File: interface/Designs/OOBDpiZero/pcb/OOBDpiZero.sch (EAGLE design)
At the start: 120 parts, among them IC10 STM32F042CT, IC11 EEPROM24, IC20 GL850G-31, IC3 DS3231, IC4 MC34063-SO, Q2 12MHz, U1 SN65HVD230(SO8), U11 STM32F042CT, U2 SN65HVD230(SO8), U4 SY6280

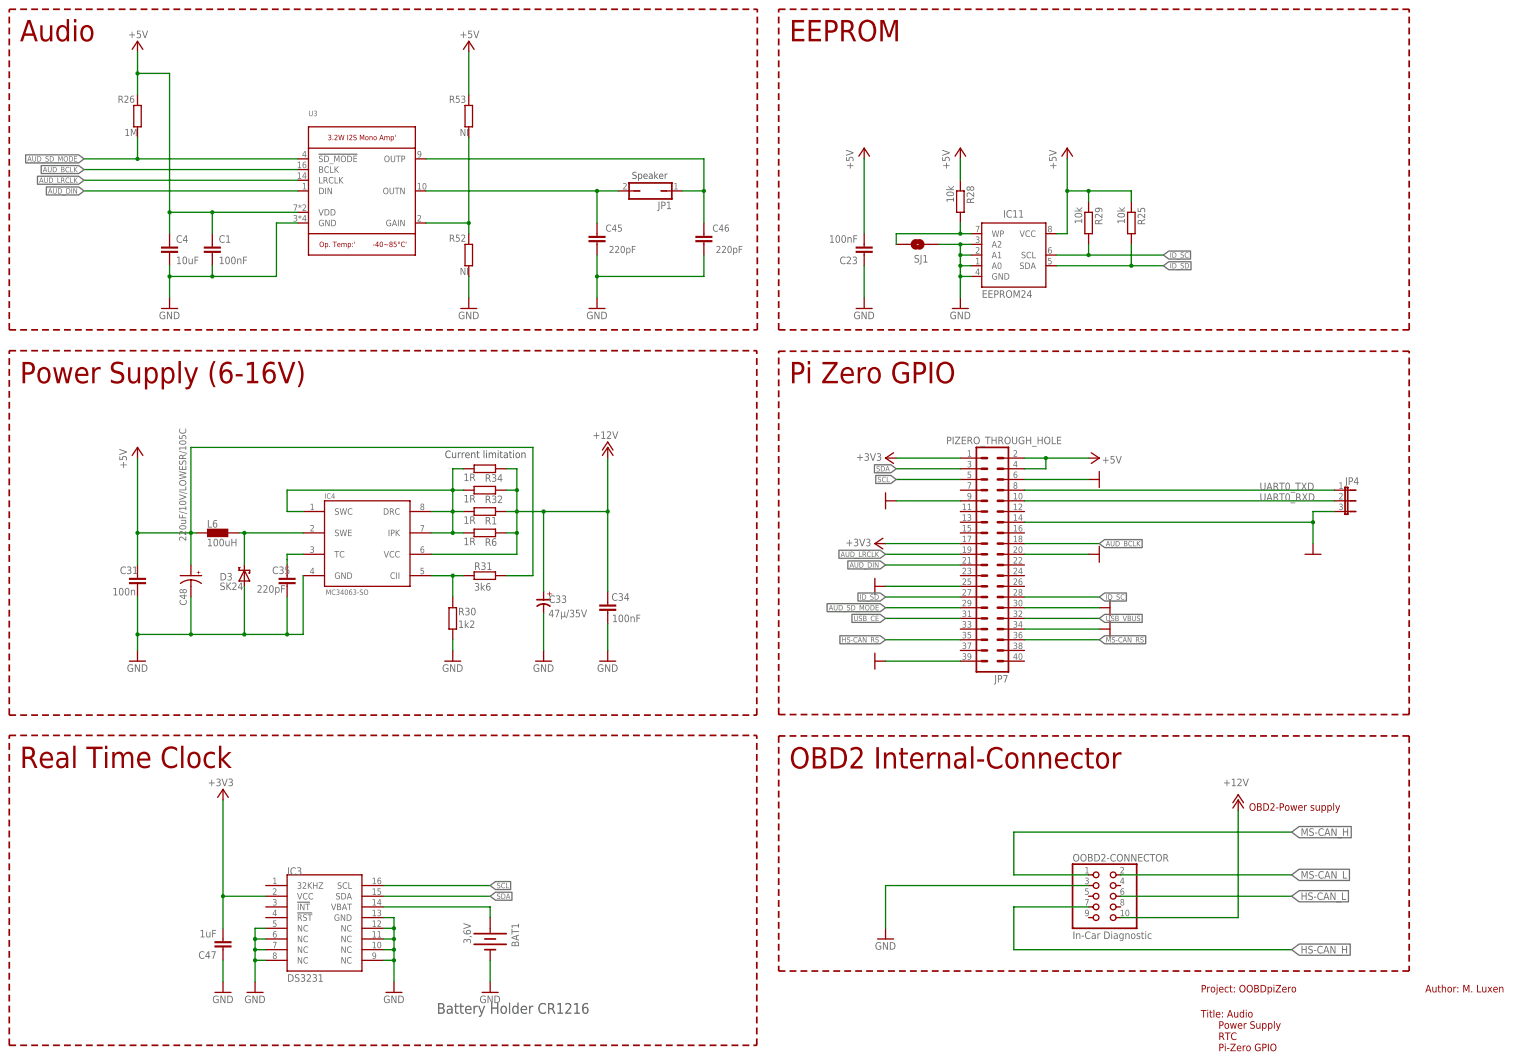
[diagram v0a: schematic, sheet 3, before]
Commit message: correct last faulty stashed commit
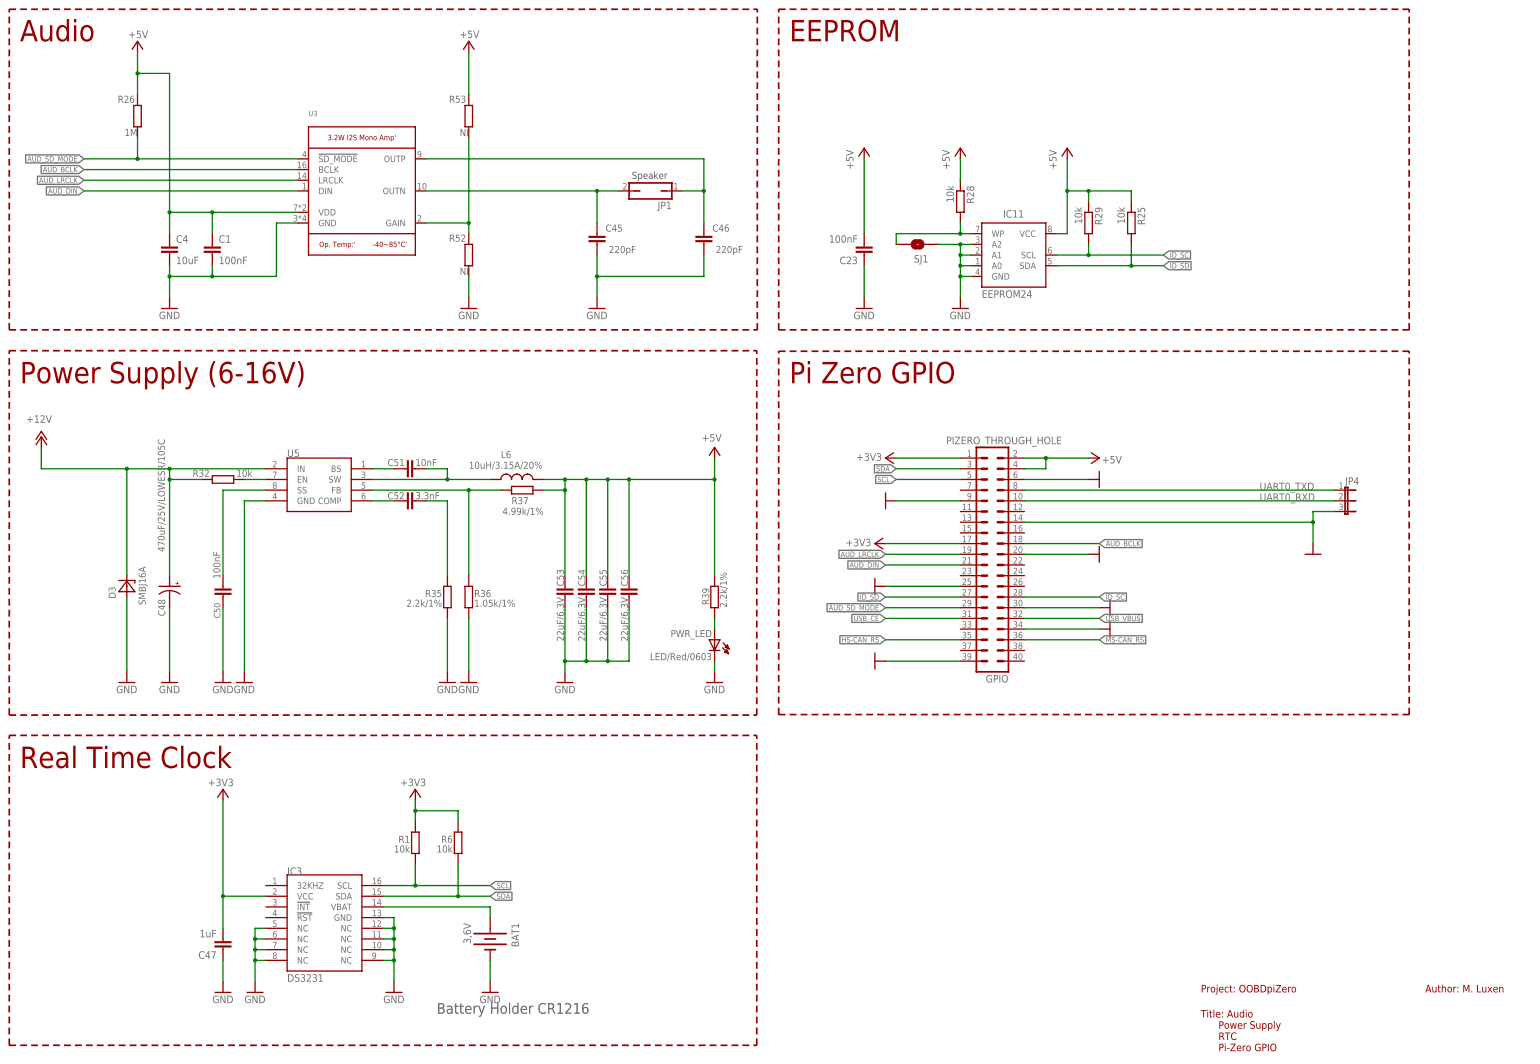
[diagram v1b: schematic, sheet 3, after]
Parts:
- removed C31: 100n, rcl:C-EUC0603K
- removed C33: 47µ/35V, cap-master:CP-SV-D
- removed C34: 100nF, rcl:C-EUC0603K
- removed C35: 220pF, rcl:C-EUC0603K
- removed IC4: MC34063-SO, mc34063:MC34063-SO
- removed OOBD2-CONNECTOR: In-Car Diagnostic, pinhead:PINHD-2X5/90
- removed R30: 1k2, rcl:R-EU_R0603
- removed R31: 3k6, rcl:R-EU_R0603
- removed R34: 1R, rcl:R-EU_R0805
- added C50: 100nF, rcl:C-EUC0603
- added C51: 10nF, rcl:C-EUC0603
- added C52: 3.3nF, rcl:C-EUC0603
- added C53, C54, C55, C56: 22uF/6.3V, rcl:C-EUC0603
- added PWR_LED: LED/Red/0603, DOUBLE-SIDE:LED0603DWS
- added R35, R39: 2.2k/1%, rcl:R-EU_R0603
- added R36: 1.05k/1%, rcl:R-EU_R0603
- added R37: 4.99k/1%, rcl:R-EU_R0603
- added U5: MP1482, OLIMEX_IC:MP1482
- C48: value 220uF/10V/LOWESR/105C -> 470uF/25V/LOWESR/105C
- D3: value SK24 -> SMBJ16A; device diode:SCHOTTKY-DIODESMD -> OLIMEX_DISCRET:SMBJ16A
- L6: value 100uH -> 10uH/3.15A/20%; device Inductor-Fastron:PIS4720 -> OLIMEX_DISCRET:LLQH88PN100M38
- R1, R32, R6: value 1R -> 10k; device rcl:R-EU_R0805 -> rcl:R-EU_R0603
- renumbered IC10 to U$3, IC20 to U$5, JP7 to GPIO, U11 to U$2
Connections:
- removed net N$1: IC4.DRC, IC4.IPK, IC4.SWC, R1.1, R32.1, R34.1, R6.1
- new net N$129: PWR_LED.A, R39.2
- new net N$62: R36.1, R37.1, U5.FB
- new net N$7: C51.1, U5.BS
- new net N$8: C51.2, L6.1, U5.SW
- new net N$9: C52.1, U5.COMP
- net +12V: now also C48.+, D3.C, R32.1, U5.IN; no longer C33.+, C34.1, IC4.VCC, OOBD2-CONNECTOR.10, R1.2, R32.2, R34.2, R6.2
- net +3V3: now also R1.1, R6.1
- net +5V: now also C53.1, C54.1, C55.1, C56.1, L6.2, R37.2, R39.1; no longer C31.1, C48.+, L6.P$1, R31.2
- net GND: now also C50.2, C53.2, C54.2, C55.2, C56.2, PWR_LED.C, R35.2, R36.2, U5.GND; no longer C31.2, C33.-, C34.2, C35.2, IC4.GND, OOBD2-CONNECTOR.3, R30.2
- net HS-CAN_H: no longer OOBD2-CONNECTOR.7
- net HS-CAN_L: no longer OOBD2-CONNECTOR.6
- net MS-CAN_H: no longer OOBD2-CONNECTOR.1
- net MS-CAN_L: no longer OOBD2-CONNECTOR.2
- net N$11: now also C52.2, R35.1; no longer C35.1, IC4.TC
- net N$4: now also C50.1, U5.SS; no longer IC4.CII, R30.1, R31.1
- net N$6: now also R32.2, U5.EN; no longer D3.C, IC4.SWE, L6.P$2
- net SCL: now also R1.2
- net SDA: now also R6.2
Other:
- note removed: "Current limitation"
- note removed: "OBD2 Internal-Connector"
- note removed: "OBD2-Power supply"
- moved on the sheet: C48, R1, R32, R6

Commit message: exchange power supply circuit to MC34063
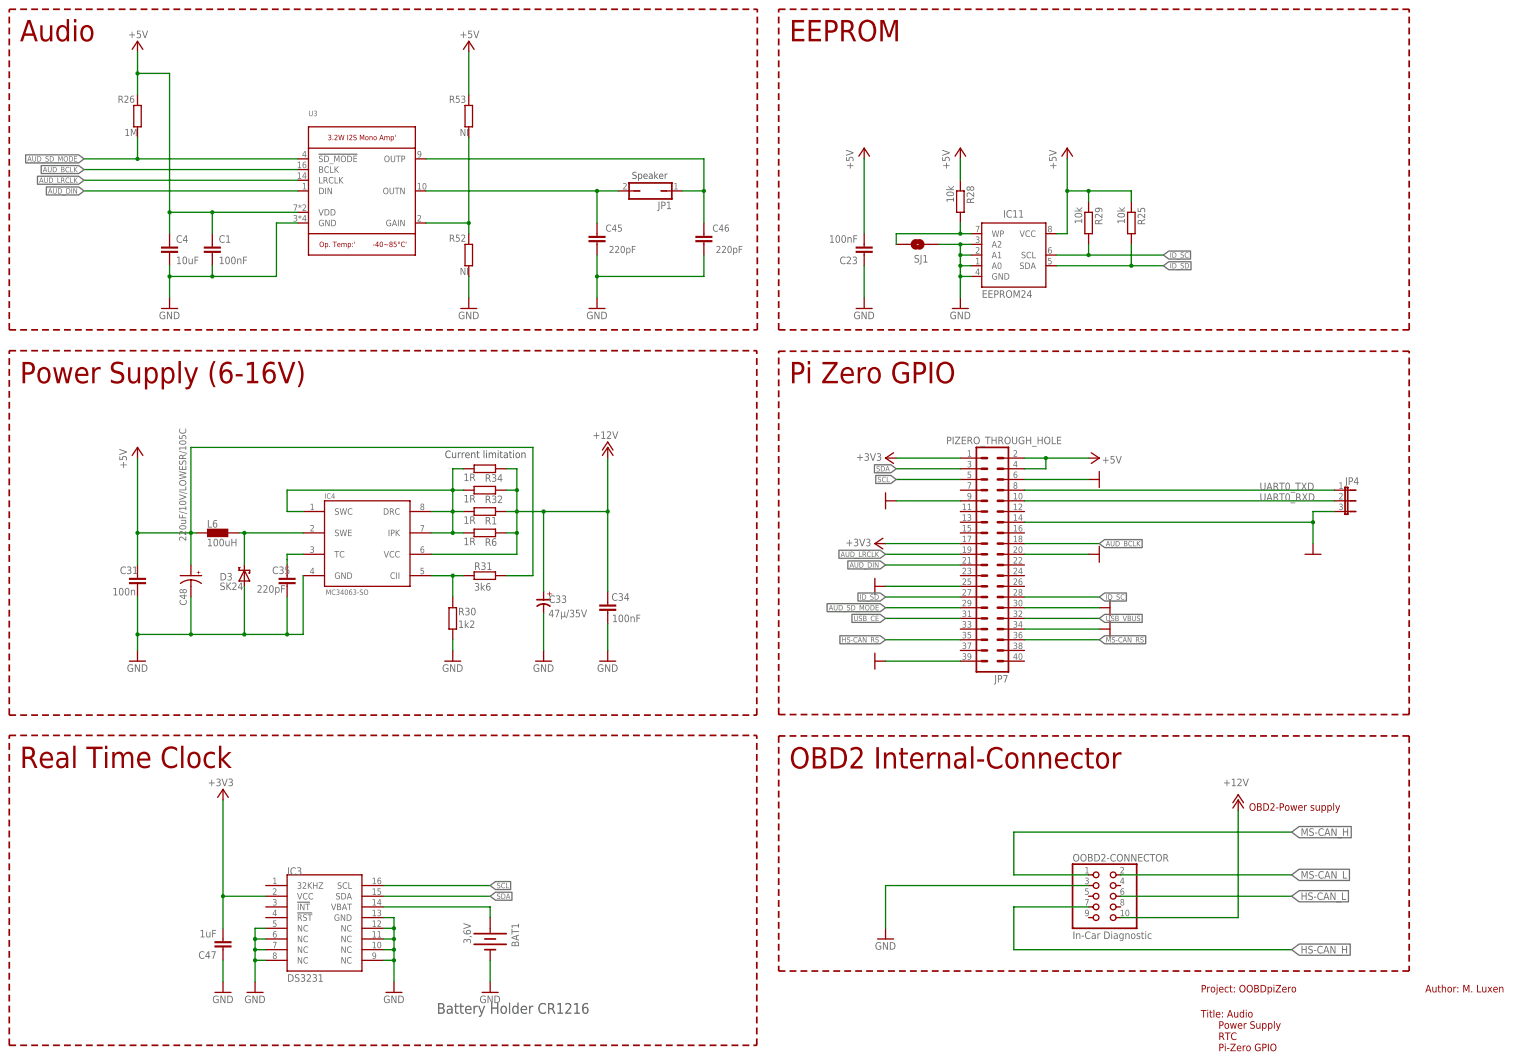
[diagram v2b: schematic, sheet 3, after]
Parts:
- removed C50: 100nF, rcl:C-EUC0603
- removed C51: 10nF, rcl:C-EUC0603
- removed C52: 3.3nF, rcl:C-EUC0603
- removed C53, C54, C55, C56: 22uF/6.3V, rcl:C-EUC0603
- removed PWR_LED: LED/Red/0603, DOUBLE-SIDE:LED0603DWS
- removed R35, R39: 2.2k/1%, rcl:R-EU_R0603
- removed R36: 1.05k/1%, rcl:R-EU_R0603
- removed R37: 4.99k/1%, rcl:R-EU_R0603
- removed U5: MP1482, OLIMEX_IC:MP1482
- added C31: 100n, rcl:C-EUC0603K
- added C33: 47µ/35V, cap-master:CP-SV-D
- added C34: 100nF, rcl:C-EUC0603K
- added C35: 220pF, rcl:C-EUC0603K
- added IC4: MC34063-SO, mc34063:MC34063-SO
- added OOBD2-CONNECTOR: In-Car Diagnostic, pinhead:PINHD-2X5/90
- added R30: 1k2, rcl:R-EU_R0603
- added R31: 3k6, rcl:R-EU_R0603
- added R34: 1R, rcl:R-EU_R0805
- C48: value 470uF/25V/LOWESR/105C -> 220uF/10V/LOWESR/105C
- D3: value SMBJ16A -> SK24; device OLIMEX_DISCRET:SMBJ16A -> diode:SCHOTTKY-DIODESMD
- L6: value 10uH/3.15A/20% -> 100uH; device OLIMEX_DISCRET:LLQH88PN100M38 -> Inductor-Fastron:PIS4720
- R1, R32, R6: value 10k -> 1R; device rcl:R-EU_R0603 -> rcl:R-EU_R0805
- renumbered GPIO to JP7, U$2 to U11, U$3 to IC10, U$5 to IC20
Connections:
- removed net N$129: PWR_LED.A, R39.2
- removed net N$62: R36.1, R37.1, U5.FB
- removed net N$7: C51.1, U5.BS
- removed net N$8: C51.2, L6.1, U5.SW
- removed net N$9: C52.1, U5.COMP
- new net N$1: IC4.DRC, IC4.IPK, IC4.SWC, R1.1, R32.1, R34.1, R6.1
- net +12V: now also C33.+, C34.1, IC4.VCC, OOBD2-CONNECTOR.10, R1.2, R32.2, R34.2, R6.2; no longer C48.+, D3.C, R32.1, U5.IN
- net +3V3: no longer R1.1, R6.1
- net +5V: now also C31.1, C48.+, L6.P$1, R31.2; no longer C53.1, C54.1, C55.1, C56.1, L6.2, R37.2, R39.1
- net GND: now also C31.2, C33.-, C34.2, C35.2, IC4.GND, OOBD2-CONNECTOR.3, R30.2; no longer C50.2, C53.2, C54.2, C55.2, C56.2, PWR_LED.C, R35.2, R36.2, U5.GND
- net HS-CAN_H: now also OOBD2-CONNECTOR.7
- net HS-CAN_L: now also OOBD2-CONNECTOR.6
- net MS-CAN_H: now also OOBD2-CONNECTOR.1
- net MS-CAN_L: now also OOBD2-CONNECTOR.2
- net N$11: now also C35.1, IC4.TC; no longer C52.2, R35.1
- net N$4: now also IC4.CII, R30.1, R31.1; no longer C50.1, U5.SS
- net N$6: now also D3.C, IC4.SWE, L6.P$2; no longer R32.2, U5.EN
- net SCL: no longer R1.2
- net SDA: no longer R6.2
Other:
- note added: "Current limitation"
- note added: "OBD2 Internal-Connector"
- note added: "OBD2-Power supply"
- moved on the sheet: C48, R1, R32, R6
